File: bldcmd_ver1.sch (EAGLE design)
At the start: 35 parts, among them IC1 STSPIN32F0, IC2 AS5047P-ATSM, Q1 PSMN2R4-30MLD, Q2 PSMN2R4-30MLD, Q3 PSMN2R4-30MLD, Q4 PSMN2R4-30MLD, Q5 PSMN2R4-30MLD, Q6 PSMN2R4-30MLD

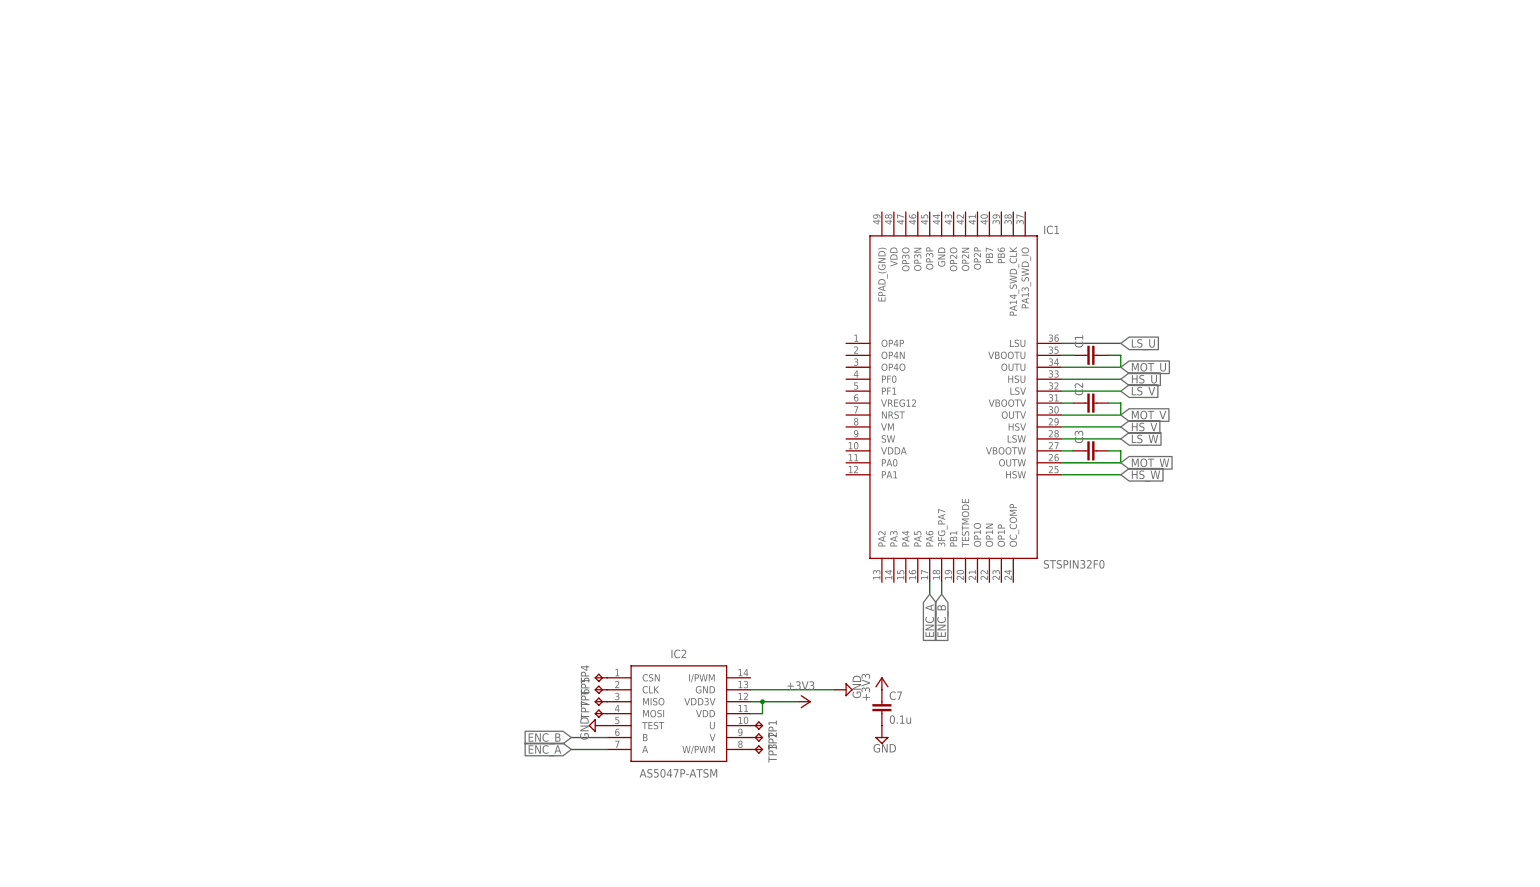
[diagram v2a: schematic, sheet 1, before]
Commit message: 部品追加
RS485トランシーバ
バックコンバータ用インダクタ
パスコン
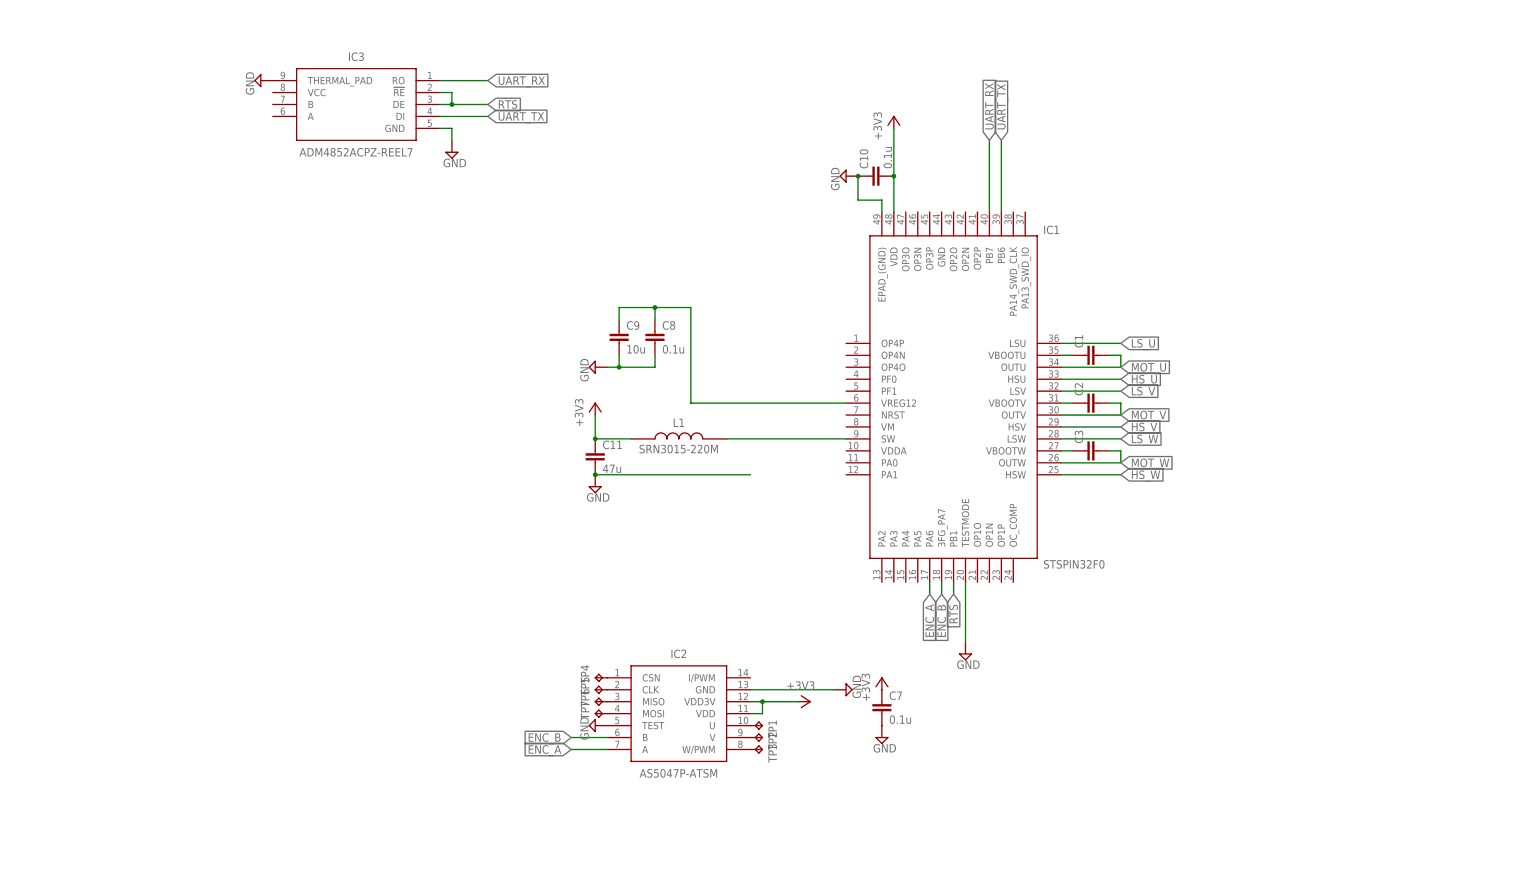
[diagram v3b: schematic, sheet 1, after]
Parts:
- added C10, C8: 0.1u, rcl:C-EUC0603K
- added C11: 47u, rcl:C-EUC1206K
- added C9: 10u, rcl:C-EUC0805K
- added IC3: ADM4852ACPZ-REEL7, rcssl_lib:ADM4852ACPZ-REEL7
- added L1: SRN3015-220M, rcssl_lib:SRN3015-220M
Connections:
- new net N$18: IC1.SW, L1.2
- new net N$19: C8.1, C9.1, IC1.VREG12
- new net RTS: IC1.PB1, IC3.!RE, IC3.DE
- new net UART_RX: IC1.PB7, IC3.RO
- new net UART_TX: IC1.PB6, IC3.DI
- net +3V3: now also C10.2, C11.1, IC1.VDD, L1.1
- net GND: now also C10.1, C11.2, C8.2, C9.2, IC1.EPAD_(GND), IC1.TESTMODE, IC3.GND, IC3.THERMAL_PAD
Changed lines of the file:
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@@
 <part name="TP7" library="testpad" library_urn="urn:adsk.eagle:library:385" deviceset="TP" device="TP06R" package3d_urn="urn:adsk.eagle:package:27954/1"/>
 <part name="SUPPLY4" library="supply2" library_urn="urn:adsk.eagle:library:372" deviceset="GND" device=""/>
+<part name="IC3" library="rcssl_lib" deviceset="ADM4852ACPZ-REEL7" device=""/>
+<part name="SUPPLY5" library="supply2" library_urn="urn:adsk.eagle:library:372" deviceset="GND" device=""/>
+<part name="SUPPLY6" library="supply2" library_urn="urn:adsk.eagle:library:372" deviceset="GND" device=""/>
+<part name="SUPPLY7" library="supply2" library_urn="urn:adsk.eagle:library:372" deviceset="GND" device=""/>
+<part name="L1" library="rcssl_lib" deviceset="SRN3015-220M" device=""/>
+<part name="SUPPLY8" library="supply2" library_urn="urn:adsk.eagle:library:372" deviceset="GND" device=""/>
+<part name="C8" library="rcl" library_urn="urn:adsk.eagle:library:334" deviceset="C-EU" device="C0603K" package3d_urn="urn:adsk.eagle:package:23680/2" value="0.1u"/>
+<part name="C9" library="rcl" library_urn="urn:adsk.eagle:library:334" deviceset="C-EU" device="C0805K" package3d_urn="urn:adsk.eagle:package:23681/2" value="10u"/>
+<part name="SUPPLY9" library="supply2" library_urn="urn:adsk.eagle:library:372" deviceset="GND" device=""/>
+<part name="C10" library="rcl" library_urn="urn:adsk.eagle:library:334" deviceset="C-EU" device="C0603K" package3d_urn="urn:adsk.eagle:package:23680/2" value="0.1u"/>
+<part name="+3V3" library="supply1" library_urn="urn:adsk.eagle:library:371" deviceset="+3V3" device=""/>
+<part name="+3V4" library="supply1" library_urn="urn:adsk.eagle:library:371" deviceset="+3V3" device=""/>
+<part name="C11" library="rcl" library_urn="urn:adsk.eagle:library:334" deviceset="C-EU" device="C1206K" package3d_urn="urn:adsk.eagle:package:23682/2" value="47u"/>
+<part name="SUPPLY10" library="supply2" library_urn="urn:adsk.eagle:library:372" deviceset="GND" device=""/>
 </parts>
 <sheets>
@@
 <instance part="TP7" gate="G$1" x="-45.72" y="-78.74" rot="R90"/>
 <instance part="SUPPLY4" gate="GND" x="-45.72" y="-81.28" rot="R270"/>
+<instance part="IC3" gate="G$1" x="-78.74" y="55.88" rot="MR0"/>
+<instance part="SUPPLY5" gate="GND" x="-76.2" y="40.64"/>
+<instance part="SUPPLY6" gate="GND" x="33.02" y="-66.04"/>
+<instance part="SUPPLY7" gate="GND" x="-116.84" y="55.88" rot="R270"/>
+<instance part="L1" gate="G$1" x="-38.1" y="-20.32"/>
+<instance part="SUPPLY8" gate="GND" x="7.62" y="35.56" rot="R270"/>
+<instance part="C8" gate="G$1" x="-33.02" y="2.54"/>
+<instance part="C9" gate="G$1" x="-40.64" y="2.54"/>
+<instance part="SUPPLY9" gate="GND" x="-45.72" y="-5.08" rot="R270"/>
+<instance part="C10" gate="G$1" x="12.7" y="35.56" rot="R90"/>
+<instance part="+3V3" gate="G$1" x="17.78" y="48.26"/>
+<instance part="+3V4" gate="G$1" x="-45.72" y="-12.7"/>
+<instance part="C11" gate="G$1" x="-45.72" y="-22.86"/>
+<instance part="SUPPLY10" gate="GND" x="-45.72" y="-30.48"/>
 </instances>
 <busses>
@@
 <pinref part="IC2" gate="G$1" pin="TEST"/>
 <pinref part="SUPPLY4" gate="GND" pin="GND"/>
+</segment>
+<segment>
+<pinref part="IC3" gate="G$1" pin="GND"/>
+<pinref part="SUPPLY5" gate="GND" pin="GND"/>
+<wire x1="-78.74" y1="45.72" x2="-76.2" y2="45.72" width="0.1524" layer="91"/>
+<wire x1="-76.2" y1="45.72" x2="-76.2" y2="43.18" width="0.1524" layer="91"/>
+</segment>
+<segment>
+<pinref part="SUPPLY6" gate="GND" pin="GND"/>
+<pinref part="IC1" gate="G$1" pin="TESTMODE"/>
+<wire x1="33.02" y1="-63.5" x2="33.02" y2="-50.8" width="0.1524" layer="91"/>
+</segment>
+<segment>
+<pinref part="IC3" gate="G$1" pin="THERMAL_PAD"/>
+<pinref part="SUPPLY7" gate="GND" pin="GND"/>
+</segment>
+<segment>
+<pinref part="SUPPLY9" gate="GND" pin="GND"/>
+<pinref part="C9" gate="G$1" pin="2"/>
+<wire x1="-43.18" y1="-5.08" x2="-40.64" y2="-5.08" width="0.1524" layer="91"/>
+<wire x1="-40.64" y1="-5.08" x2="-40.64" y2="-2.54" width="0.1524" layer="91"/>
+<pinref part="C8" gate="G$1" pin="2"/>
+<wire x1="-40.64" y1="-5.08" x2="-33.02" y2="-5.08" width="0.1524" layer="91"/>
+<wire x1="-33.02" y1="-5.08" x2="-33.02" y2="-2.54" width="0.1524" layer="91"/>
+<junction x="-40.64" y="-5.08"/>
+</segment>
+<segment>
+<pinref part="IC1" gate="G$1" pin="EPAD_(GND)"/>
+<wire x1="15.24" y1="27.94" x2="15.24" y2="30.48" width="0.1524" layer="91"/>
+<wire x1="15.24" y1="30.48" x2="10.16" y2="30.48" width="0.1524" layer="91"/>
+<pinref part="C10" gate="G$1" pin="1"/>
+<wire x1="10.16" y1="30.48" x2="10.16" y2="35.56" width="0.1524" layer="91"/>
+<pinref part="SUPPLY8" gate="GND" pin="GND"/>
+<junction x="10.16" y="35.56"/>
+</segment>
+<segment>
+<pinref part="C11" gate="G$1" pin="2"/>
+<pinref part="SUPPLY10" gate="GND" pin="GND"/>
+<wire x1="-45.72" y1="-27.94" x2="-12.7" y2="-27.94" width="0.1524" layer="91"/>
+<junction x="-45.72" y="-27.94"/>
 </segment>
 </net>
@@
 <pinref part="+3V2" gate="G$1" pin="+3V3"/>
 </segment>
+<segment>
+<pinref part="C10" gate="G$1" pin="2"/>
+<pinref part="IC1" gate="G$1" pin="VDD"/>
+<wire x1="17.78" y1="35.56" x2="17.78" y2="27.94" width="0.1524" layer="91"/>
+<pinref part="+3V3" gate="G$1" pin="+3V3"/>
+<wire x1="17.78" y1="45.72" x2="17.78" y2="35.56" width="0.1524" layer="91"/>
+<junction x="17.78" y="35.56"/>
+</segment>
+<segment>
+<pinref part="+3V4" gate="G$1" pin="+3V3"/>
+<wire x1="-45.72" y1="-15.24" x2="-45.72" y2="-20.32" width="0.1524" layer="91"/>
+<pinref part="L1" gate="G$1" pin="1"/>
+<wire x1="-45.72" y1="-20.32" x2="-38.1" y2="-20.32" width="0.1524" layer="91"/>
+<pinref part="C11" gate="G$1" pin="1"/>
+<junction x="-45.72" y="-20.32"/>
+</segment>
 </net>
 <net name="ENC_B" class="0">
@@
 </segment>
 </net>
+<net name="UART_TX" class="0">
+<segment>
+<pinref part="IC1" gate="G$1" pin="PB6"/>
+<wire x1="40.64" y1="27.94" x2="40.64" y2="43.18" width="0.1524" layer="91"/>
+<label x="40.64" y="43.18" size="1.778" layer="95" rot="R90" xref="yes"/>
+</segment>
+<segment>
+<pinref part="IC3" gate="G$1" pin="DI"/>
+<wire x1="-78.74" y1="48.26" x2="-68.58" y2="48.26" width="0.1524" layer="91"/>
+<label x="-68.58" y="48.26" size="1.778" layer="95" xref="yes"/>
+</segment>
+</net>
+<net name="UART_RX" class="0">
+<segment>
+<pinref part="IC1" gate="G$1" pin="PB7"/>
+<wire x1="38.1" y1="27.94" x2="38.1" y2="43.18" width="0.1524" layer="91"/>
+<label x="38.1" y="43.18" size="1.778" layer="95" rot="R90" xref="yes"/>
+</segment>
+<segment>
+<pinref part="IC3" gate="G$1" pin="RO"/>
+<wire x1="-78.74" y1="55.88" x2="-68.58" y2="55.88" width="0.1524" layer="91"/>
+<label x="-68.58" y="55.88" size="1.778" layer="95" xref="yes"/>
+</segment>
+</net>
+<net name="RTS" class="0">
+<segment>
+<pinref part="IC3" gate="G$1" pin="!RE"/>
+<wire x1="-78.74" y1="53.34" x2="-76.2" y2="53.34" width="0.1524" layer="91"/>
+<wire x1="-76.2" y1="53.34" x2="-76.2" y2="50.8" width="0.1524" layer="91"/>
+<pinref part="IC3" gate="G$1" pin="DE"/>
+<wire x1="-76.2" y1="50.8" x2="-78.74" y2="50.8" width="0.1524" layer="91"/>
+<wire x1="-76.2" y1="50.8" x2="-68.58" y2="50.8" width="0.1524" layer="91"/>
+<junction x="-76.2" y="50.8"/>
+<label x="-68.58" y="50.8" size="1.778" layer="95" xref="yes"/>
+</segment>
+<segment>
+<pinref part="IC1" gate="G$1" pin="PB1"/>
+<wire x1="30.48" y1="-50.8" x2="30.48" y2="-53.34" width="0.1524" layer="91"/>
+<label x="30.48" y="-53.34" size="1.778" layer="95" rot="R270" xref="yes"/>
+</segment>
+</net>
+<net name="N$18" class="0">
+<segment>
+<pinref part="L1" gate="G$1" pin="2"/>
+<wire x1="-17.78" y1="-20.32" x2="7.62" y2="-20.32" width="0.1524" layer="91"/>
+<pinref part="IC1" gate="G$1" pin="SW"/>
+</segment>
+</net>
+<net name="N$19" class="0">
+<segment>
+<pinref part="IC1" gate="G$1" pin="VREG12"/>
+<wire x1="7.62" y1="-12.7" x2="-25.4" y2="-12.7" width="0.1524" layer="91"/>
+<wire x1="-25.4" y1="-12.7" x2="-25.4" y2="7.62" width="0.1524" layer="91"/>
+<pinref part="C9" gate="G$1" pin="1"/>
+<wire x1="-25.4" y1="7.62" x2="-33.02" y2="7.62" width="0.1524" layer="91"/>
+<wire x1="-33.02" y1="7.62" x2="-40.64" y2="7.62" width="0.1524" layer="91"/>
+<wire x1="-40.64" y1="7.62" x2="-40.64" y2="5.08" width="0.1524" layer="91"/>
+<pinref part="C8" gate="G$1" pin="1"/>
+<wire x1="-33.02" y1="5.08" x2="-33.02" y2="7.62" width="0.1524" layer="91"/>
+<junction x="-33.02" y="7.62"/>
+</segment>
+</net>

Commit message: 部品追加
モータ出力コネクタ
ネジ穴
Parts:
- added H1, H2, H3, H4: MOUNT-PAD-ROUND3.2, holes:MOUNT-PAD-ROUND3.2
- added J1: DF65-3P-1.7V(21), rcssl_lib:DF65-3P-1.7V(21)
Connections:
- net MOT_U: now also J1.1
- net MOT_V: now also J1.2
- net MOT_W: now also J1.3
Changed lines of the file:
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@@
 <part name="C11" library="rcl" library_urn="urn:adsk.eagle:library:334" deviceset="C-EU" device="C1206K" package3d_urn="urn:adsk.eagle:package:23682/2" value="47u"/>
 <part name="SUPPLY10" library="supply2" library_urn="urn:adsk.eagle:library:372" deviceset="GND" device=""/>
+<part name="J1" library="rcssl_lib" deviceset="DF65-3P-1.7V(21)" device=""/>
+<part name="H1" library="holes" library_urn="urn:adsk.eagle:library:237" deviceset="MOUNT-PAD-ROUND" device="3.2" package3d_urn="urn:adsk.eagle:package:14282/1"/>
+<part name="H2" library="holes" library_urn="urn:adsk.eagle:library:237" deviceset="MOUNT-PAD-ROUND" device="3.2" package3d_urn="urn:adsk.eagle:package:14282/1"/>
+<part name="H3" library="holes" library_urn="urn:adsk.eagle:library:237" deviceset="MOUNT-PAD-ROUND" device="3.2" package3d_urn="urn:adsk.eagle:package:14282/1"/>
+<part name="H4" library="holes" library_urn="urn:adsk.eagle:library:237" deviceset="MOUNT-PAD-ROUND" device="3.2" package3d_urn="urn:adsk.eagle:package:14282/1"/>
 </parts>
 <sheets>
@@
 <instance part="C11" gate="G$1" x="-45.72" y="-22.86"/>
 <instance part="SUPPLY10" gate="GND" x="-45.72" y="-30.48"/>
+<instance part="H1" gate="G$1" x="81.28" y="-73.66"/>
+<instance part="H2" gate="G$1" x="81.28" y="-78.74"/>
+<instance part="H3" gate="G$1" x="81.28" y="-83.82"/>
+<instance part="H4" gate="G$1" x="81.28" y="-88.9"/>
 </instances>
 <busses>
@@
 <instance part="R13" gate="G$1" x="96.52" y="22.86" rot="R90"/>
 <instance part="SUPPLY1" gate="GND" x="96.52" y="10.16"/>
+<instance part="J1" gate="G$1" x="226.06" y="60.96"/>
 </instances>
 <busses>
@@
 <label x="30.48" y="60.96" size="1.778" layer="95" xref="yes"/>
 </segment>
+<segment>
+<pinref part="J1" gate="G$1" pin="1"/>
+<wire x1="226.06" y1="60.96" x2="223.52" y2="60.96" width="0.1524" layer="91"/>
+<label x="223.52" y="60.96" size="1.778" layer="95" rot="R180" xref="yes"/>
+</segment>
 </net>
 <net name="MOT_V" class="0">
@@
 <label x="99.06" y="60.96" size="1.778" layer="95" xref="yes"/>
 </segment>
+<segment>
+<pinref part="J1" gate="G$1" pin="2"/>
+<wire x1="246.38" y1="60.96" x2="248.92" y2="60.96" width="0.1524" layer="91"/>
+<label x="248.92" y="60.96" size="1.778" layer="95" xref="yes"/>
+</segment>
 </net>
 <net name="MOT_W" class="0">
@@
 <wire x1="167.64" y1="60.96" x2="170.18" y2="60.96" width="0.1524" layer="91"/>
 </segment>
-</net>
+<segment>
+<pinref part="J1" gate="G$1" pin="3"/>
+<wire x1="226.06" y1="58.42" x2="223.52" y2="58.42" width="0.1524" layer="91"/>
+<label x="223.52" y="58.42" size="1.778" layer="95" rot="R180" xref="yes"/>
+</segment>
+</net>
